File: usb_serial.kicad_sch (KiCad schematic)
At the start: 3 parts, among them U5 CP2104-F03-GM

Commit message: laid out stuff
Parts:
- added C17, C18: 1uF, Capacitor_SMD:C_0805_2012Metric_Pad1.18x1.45mm_HandSolder, symbol Device:C
- U5: Availability In Stock -> (none); Check_prices https://www.snapeda.com/parts/CP2104-F03-GM/Silicon+Labs/vi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 -> (none); MANUFACTURER Silicon Labs -> (none); MF Silicon Labs -> (none); MP CP2104-F03-GM -> (none); PARTREV 1.2 -> (none); Package QFN-24 Silicon Labs -> (none); Price None -> (none); Purchase-URL https://www.snapeda.com/api/url_track_click_mouser/?unipart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 -> (none); STANDARD IPC7351B -> (none); SnapEDA_Link https://www.snapeda.com/parts/CP2104-F03-GM/Silicon+Labs/vi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 -> (none)
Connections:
- net +5V: now also U5.7 (REGIN), C18.1
- net GND: now also C17.2, C18.2
- net at U5.16 (VPP): now also C17.1
- net +3.3V renamed +3V3
- net +3V3: no longer U5.7 (REGIN)
- no-connect marks 12 -> 11
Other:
- note added: "Note: +3V3 is for the CP2104 ONLY, +3.3V is for the ESP32 ONLY"
- moved on the sheet: C10, C9

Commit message: neat-ified schematics
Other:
- company: (none) -> The Art and Science of PCB Design
- title: (none) -> RGB LED Driver Demo Board
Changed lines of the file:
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@@
   (paper "USLetter")
   (title_block
+    (title "RGB LED Driver Demo Board")
     (date "2024-01-01")
     (rev "A01")
+    (company "The Art and Science of PCB Design")
   )
   (junction (at 113.665 71.12) (diameter 0) (color 0 0 0 0)

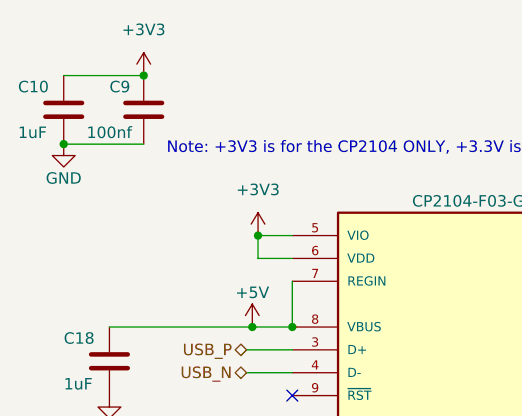
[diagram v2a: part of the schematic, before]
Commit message: Added annotations, BOM count reduction
LED indicator resistors edited to save on BOM count

schematics made more neat, added some labels
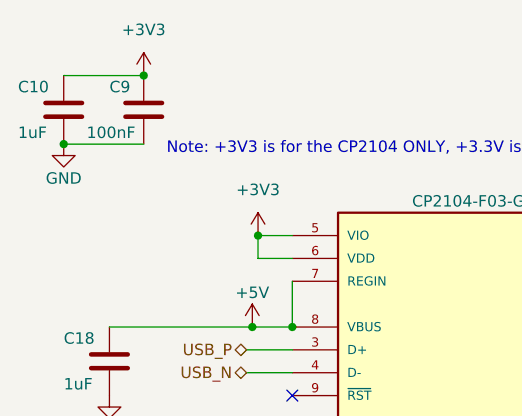
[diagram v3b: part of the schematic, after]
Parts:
- C9: value 100nf -> 100nF
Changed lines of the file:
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@@
       (effects (font (size 1.27 1.27)) (justify left))
     )
-    (property "Value" "100nf" (at 95.25 49.53 0)
+    (property "Value" "100nF" (at 95.25 49.53 0)
       (effects (font (size 1.27 1.27)) (justify left))
     )

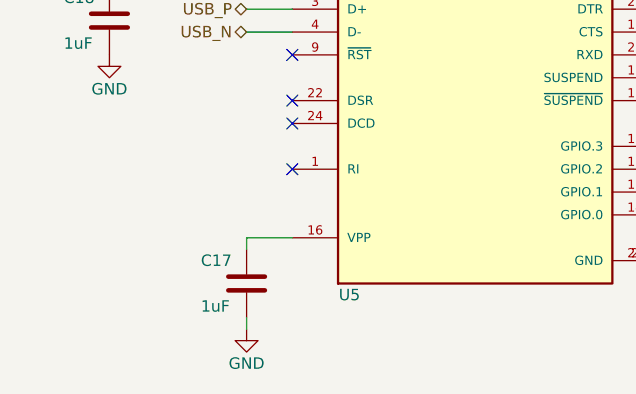
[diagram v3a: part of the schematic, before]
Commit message: added digikey PNs
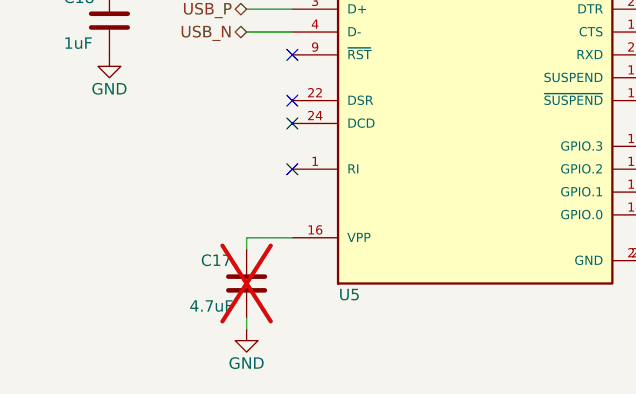
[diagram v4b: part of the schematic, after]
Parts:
- C10, C18, C9: Digikey PN (none) -> 1276-1003-1-ND; MPN (none) -> CL21B104KBCNNNC
- C17: value 1uF -> 4.7uF; Digikey PN (none) -> 445-5980-1-ND; MPN (none) -> C2012X5R1H475K125AB; now not fitted
- U5: Digikey PN (none) -> 336-4146-1-ND; MPN (none) -> CP2104-F03-GM
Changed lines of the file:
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@@
       (effects (font (size 1.27 1.27)) hide)
     )
-    (property "Digikey PN" "" (at 101.6 46.99 0)
+    (property "Digikey PN" "1276-1003-1-ND" (at 101.6 46.99 0)
+      (effects (font (size 1.27 1.27)) hide)
+    )
+    (property "MPN" "CL21B104KBCNNNC" (at 101.6 46.99 0)
       (effects (font (size 1.27 1.27)) hide)
     )
@@
       (effects (font (size 1.27 1.27)) hide)
     )
-    (property "Digikey PN" "" (at 138.43 81.28 0)
+    (property "Digikey PN" "336-4146-1-ND" (at 138.43 81.28 0)
+      (effects (font (size 1.27 1.27)) hide)
+    )
+    (property "MPN" "CP2104-F03-GM" (at 138.43 81.28 0)
       (effects (font (size 1.27 1.27)) hide)
     )
@@
       (effects (font (size 1.27 1.27)) hide)
     )
-    (property "Digikey PN" "" (at 92.71 46.99 0)
+    (property "Digikey PN" "1276-1003-1-ND" (at 92.71 46.99 0)
+      (effects (font (size 1.27 1.27)) hide)
+    )
+    (property "MPN" "CL21B104KBCNNNC" (at 92.71 46.99 0)
       (effects (font (size 1.27 1.27)) hide)
     )
@@
       (effects (font (size 1.27 1.27)) hide)
     )
-    (property "Digikey PN" "" (at 97.79 74.93 0)
+    (property "Digikey PN" "1276-1003-1-ND" (at 97.79 74.93 0)
+      (effects (font (size 1.27 1.27)) hide)
+    )
+    (property "MPN" "CL21B104KBCNNNC" (at 97.79 74.93 0)
       (effects (font (size 1.27 1.27)) hide)
     )
@@
   )
   (symbol (lib_id "Device:C") (at 113.03 104.14 0) (unit 1)
-    (in_bom yes) (on_board yes) (dnp no)
+    (in_bom yes) (on_board yes) (dnp yes)
     (property "Reference" "C17" (at 107.95 101.6 0)
       (effects (font (size 1.27 1.27)) (justify left))
     )
-    (property "Value" "1uF" (at 107.95 106.68 0)
+    (property "Value" "4.7uF" (at 106.68 106.68 0)
       (effects (font (size 1.27 1.27)) (justify left))
     )
@@
       (effects (font (size 1.27 1.27)) hide)
     )
-    (property "Digikey PN" "" (at 113.03 104.14 0)
-      (effects (font (size 1.27 1.27)) hide)
-    )
+    (property "Digikey PN" "445-5980-1-ND" (at 113.03 104.14 0)
+      (effects (font (size 1.27 1.27)) hide)
+    )
+    (property "MPN" "C2012X5R1H475K125AB" (at 113.03 104.14 0)
+      (effects (font (size 1.27 1.27)) hide)
+    )

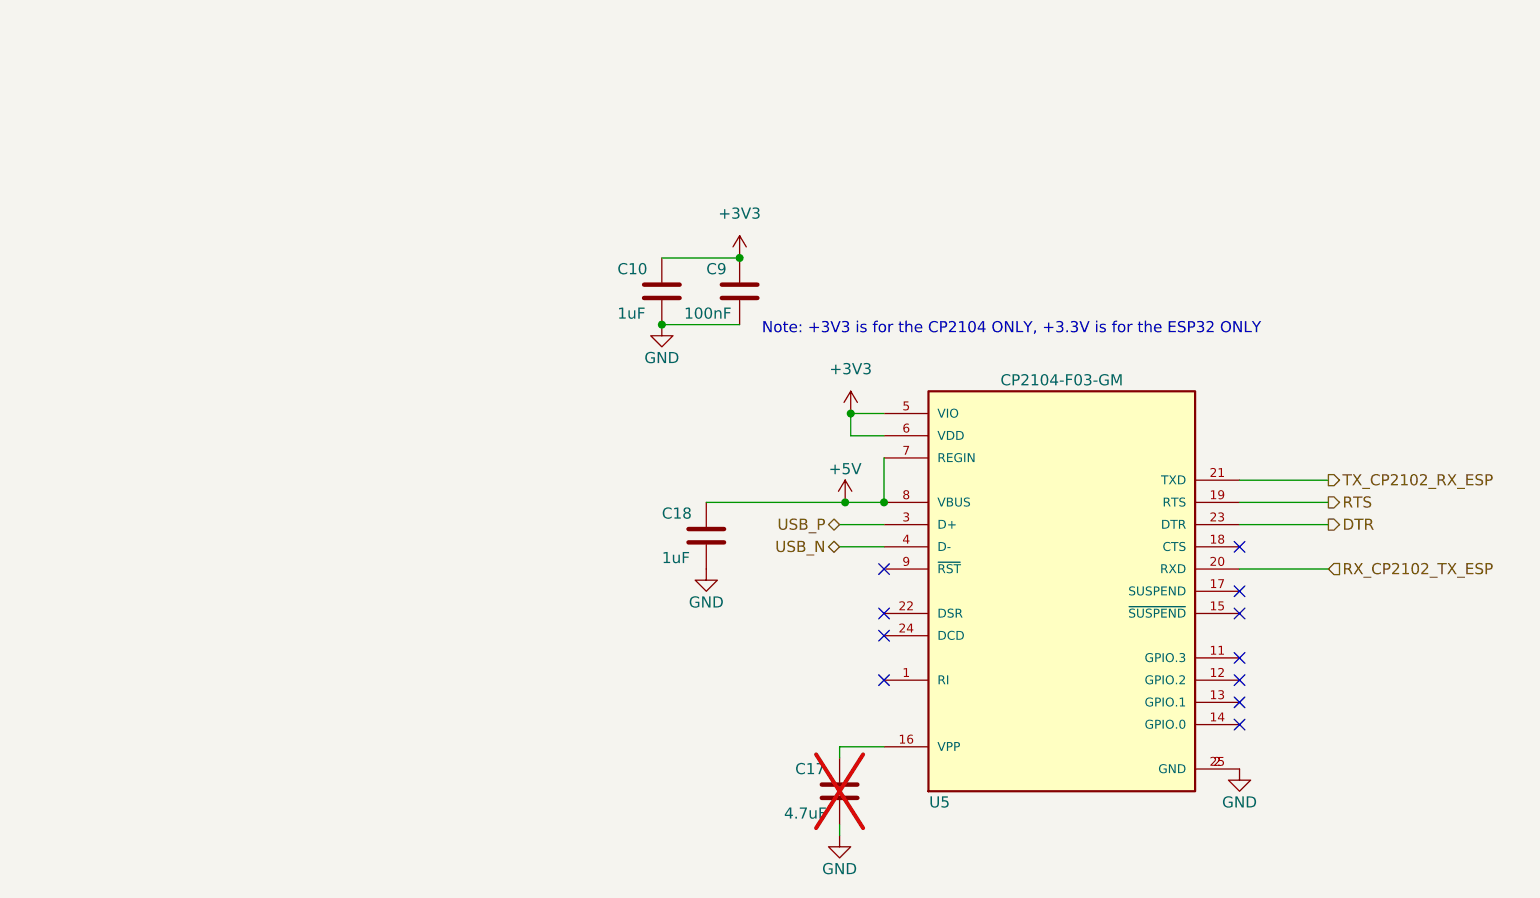
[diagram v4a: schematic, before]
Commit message: [A02] Initial release
CP2014 -> CP2012N (BOM cost reduction)
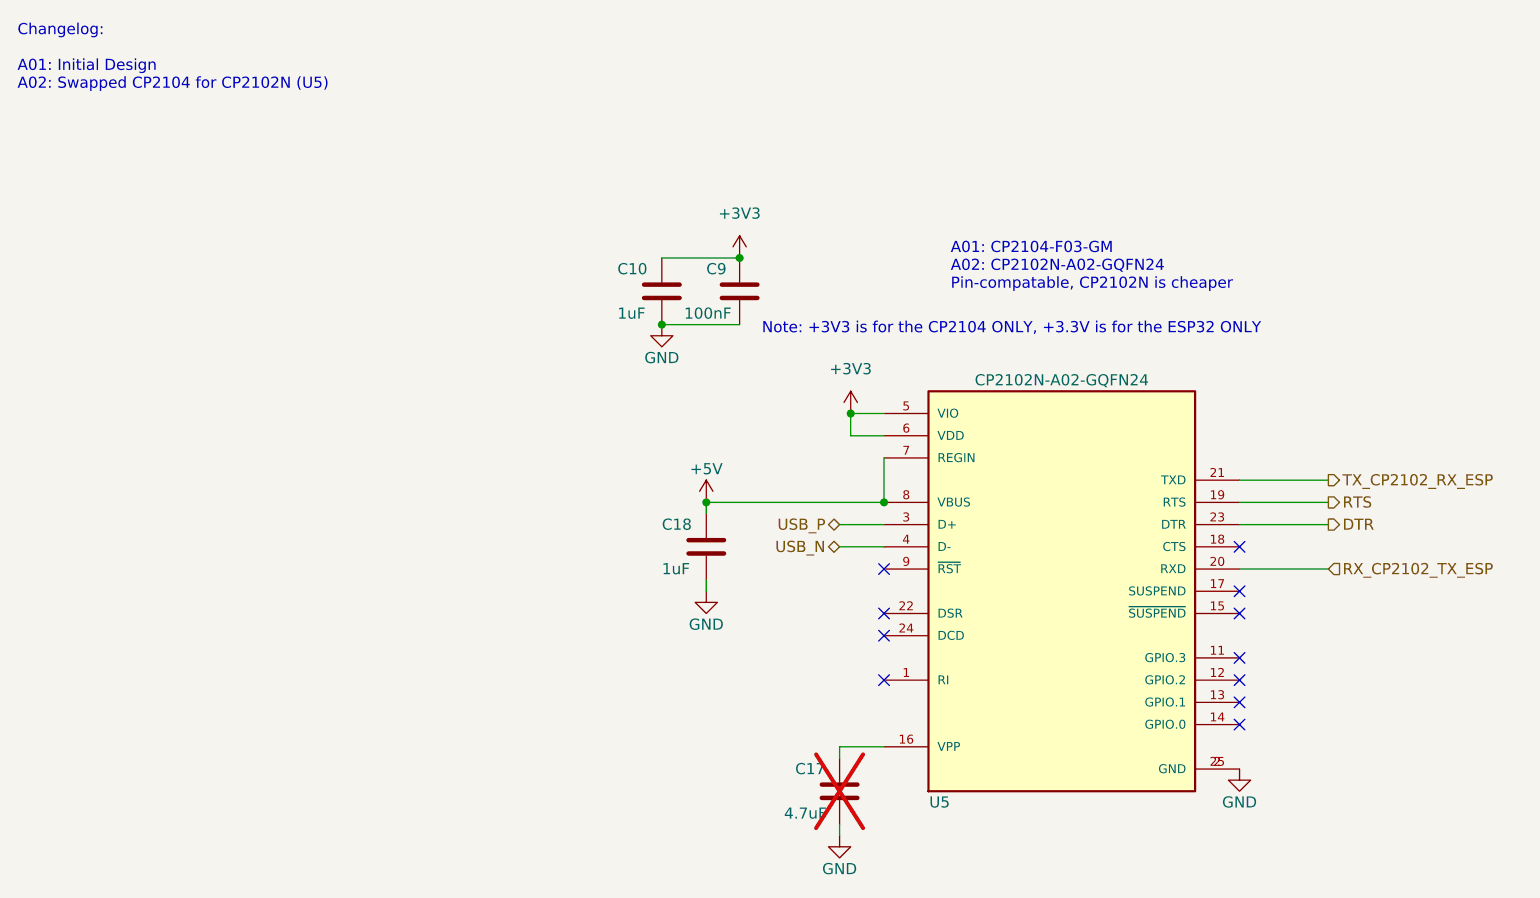
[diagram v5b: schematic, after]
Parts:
- U5: value CP2104-F03-GM -> CP2102N-A02-GQFN24; MPN CP2104-F03-GM -> CP2102N-A02-GQFN24
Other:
- note added: "A01: CP2104-F03-GM A02: CP2102N-A02-GQFN24 Pin-compatable, CP2102N is cheaper"
- note added: "Changelog: A01: Initial Design A02: Swapped CP2104 for CP2102N (U5)"
- moved on the sheet: C18
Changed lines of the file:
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@@
   (title_block
     (title "RGB LED Driver Demo Board")
-    (date "2024-01-01")
-    (rev "A01")
+    (date "2024-01-02")
+    (rev "A02")
     (company "The Art and Science of PCB Design")
   )
-  (junction (at 113.665 71.12) (diameter 0) (color 0 0 0 0)
-  )
   (junction (at 92.71 50.8) (diameter 0) (color 0 0 0 0)
   )
@@
   )
   (junction (at 118.11 71.12) (diameter 0) (color 0 0 0 0)
+  )
+  (junction (at 97.79 71.12) (diameter 0) (color 0 0 0 0)
   )
   (no_connect (at 158.75 76.2))
@@
     (stroke (width 0) (type default))
   )
-  (wire (pts (xy 113.665 71.12) (xy 118.11 71.12))
+  (wire (pts (xy 97.79 71.12) (xy 118.11 71.12))
     (stroke (width 0) (type default))
   )
@@
     (stroke (width 0) (type default))
   )
-  (wire (pts (xy 97.79 71.12) (xy 113.665 71.12))
+  (wire (pts (xy 97.79 72.39) (xy 97.79 71.12))
     (stroke (width 0) (type default))
   )
   (wire (pts (xy 158.75 78.74) (xy 168.91 78.74))
+    (stroke (width 0) (type default))
+  )
+  (wire (pts (xy 97.79 81.28) (xy 97.79 80.01))
     (stroke (width 0) (type default))
   )
@@
     (effects (font (size 1.27 1.27)) (justify left bottom))
   )
+  (text "A01: CP2104-F03-GM\nA02: CP2102N-A02-GQFN24\nPin-compatable, CP2102N is cheaper"
+    (at 125.73 46.99 0)
+    (effects (font (size 1.27 1.27)) (justify left bottom))
+  )
+  (text "Changelog:\n\nA01: Initial Design\nA02: Swapped CP2104 for CP2102N (U5)"
+    (at 19.05 24.13 0)
+    (effects (font (size 1.27 1.27)) (justify left bottom))
+  )
   (hierarchical_label "DTR" (shape output) (at 168.91 73.66 0) (fields_autoplaced)
     (effects (font (size 1.27 1.27)) (justify left))
@@
     )
   )
-  (symbol (lib_id "power:GND") (at 97.79 78.74 0) (unit 1)
-    (in_bom yes) (on_board yes) (dnp no)
-    (property "Reference" "#PWR061" (at 97.79 85.09 0)
-      (effects (font (size 1.27 1.27)) hide)
-    )
-    (property "Value" "GND" (at 97.79 82.55 0)
-      (effects (font (size 1.27 1.27)))
-    )
-    (property "Footprint" "" (at 97.79 78.74 0)
-      (effects (font (size 1.27 1.27)) hide)
-    )
-    (property "Datasheet" "" (at 97.79 78.74 0)
+  (symbol (lib_id "power:GND") (at 97.79 81.28 0) (unit 1)
+    (in_bom yes) (on_board yes) (dnp no)
+    (property "Reference" "#PWR061" (at 97.79 87.63 0)
+      (effects (font (size 1.27 1.27)) hide)
+    )
+    (property "Value" "GND" (at 97.79 85.09 0)
+      (effects (font (size 1.27 1.27)))
+    )
+    (property "Footprint" "" (at 97.79 81.28 0)
+      (effects (font (size 1.27 1.27)) hide)
+    )
+    (property "Datasheet" "" (at 97.79 81.28 0)
       (effects (font (size 1.27 1.27)) hide)
     )
@@
     )
   )
-  (symbol (lib_id "power:+5V") (at 113.665 71.12 0) (unit 1)
-    (in_bom yes) (on_board yes) (dnp no)
-    (property "Reference" "#PWR046" (at 113.665 74.93 0)
-      (effects (font (size 1.27 1.27)) hide)
-    )
-    (property "Value" "+5V" (at 113.665 67.31 0)
-      (effects (font (size 1.27 1.27)))
-    )
-    (property "Footprint" "" (at 113.665 71.12 0)
-      (effects (font (size 1.27 1.27)) hide)
-    )
-    (property "Datasheet" "" (at 113.665 71.12 0)
+  (symbol (lib_id "power:+5V") (at 97.79 71.12 0) (unit 1)
+    (in_bom yes) (on_board yes) (dnp no)
+    (property "Reference" "#PWR046" (at 97.79 74.93 0)
+      (effects (font (size 1.27 1.27)) hide)
+    )
+    (property "Value" "+5V" (at 97.79 67.31 0)
+      (effects (font (size 1.27 1.27)))
+    )
+    (property "Footprint" "" (at 97.79 71.12 0)
+      (effects (font (size 1.27 1.27)) hide)
+    )
+    (property "Datasheet" "" (at 97.79 71.12 0)
       (effects (font (size 1.27 1.27)) hide)
     )
@@
       (effects (font (size 1.27 1.27)))
     )
-    (property "Value" "CP2104-F03-GM" (at 138.43 57.15 0)
+    (property "Value" "CP2102N-A02-GQFN24" (at 138.43 57.15 0)
       (effects (font (size 1.27 1.27)))
     )
@@
       (effects (font (size 1.27 1.27)) (justify bottom) hide)
     )
-    (property "Datasheet" "" (at 138.43 81.28 0)
+    (property "Datasheet" "https://www.silabs.com/documents/public/data-sheets/cp2102n-datasheet.pdf" (at 138.43 81.28 0)
       (effects (font (size 1.27 1.27)) hide)
     )
@@
       (effects (font (size 1.27 1.27)) hide)
     )
-    (property "MPN" "CP2104-F03-GM" (at 138.43 81.28 0)
+    (property "MPN" "CP2102N-A02-GQFN24" (at 138.43 81.28 0)
       (effects (font (size 1.27 1.27)) hide)
     )
@@
     )
   )
-  (symbol (lib_id "Device:C") (at 97.79 74.93 0) (unit 1)
-    (in_bom yes) (on_board yes) (dnp no)
-    (property "Reference" "C18" (at 92.71 72.39 0)
-      (effects (font (size 1.27 1.27)) (justify left))
-    )
-    (property "Value" "1uF" (at 92.71 77.47 0)
-      (effects (font (size 1.27 1.27)) (justify left))
-    )
-    (property "Footprint" "Capacitor_SMD:C_0805_2012Metric_Pad1.18x1.45mm_HandSolder" (at 98.7552 78.74 0)
-      (effects (font (size 1.27 1.27)) hide)
-    )
-    (property "Datasheet" "~" (at 97.79 74.93 0)
-      (effects (font (size 1.27 1.27)) hide)
-    )
-    (property "Digikey PN" "1276-1003-1-ND" (at 97.79 74.93 0)
-      (effects (font (size 1.27 1.27)) hide)
-    )
-    (property "MPN" "CL21B104KBCNNNC" (at 97.79 74.93 0)
-      (effects (font (size 1.27 1.27)) hide)
-    )
+  (symbol (lib_id "Device:C") (at 97.79 76.2 0) (unit 1)
+    (in_bom yes) (on_board yes) (dnp no)
+    (property "Reference" "C18" (at 92.71 73.66 0)
+      (effects (font (size 1.27 1.27)) (justify left))
+    )
+    (property "Value" "1uF" (at 92.71 78.74 0)
+      (effects (font (size 1.27 1.27)) (justify left))
+    )
+    (property "Footprint" "Capacitor_SMD:C_0805_2012Metric_Pad1.18x1.45mm_HandSolder" (at 98.7552 80.01 0)
+      (effects (font (size 1.27 1.27)) hide)
+    )
+    (property "Datasheet" "~" (at 97.79 76.2 0)
+      (effects (font (size 1.27 1.27)) hide)
+    )
+    (property "Digikey PN" "1276-1003-1-ND" (at 97.79 76.2 0)
+      (effects (font (size 1.27 1.27)) hide)
+    )
+    (property "MPN" "CL21B104KBCNNNC" (at 97.79 76.2 0)
+      (effects (font (size 1.27 1.27)) hide)
+    )

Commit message: cost reduction in BOM
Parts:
- C10, C18: Digikey PN 1276-1003-1-ND -> 1276-1029-1-ND; MPN CL21B104KBCNNNC -> CL21B105KBFNNNE
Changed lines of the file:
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@@
       (effects (font (size 1.27 1.27)) hide)
     )
-    (property "Digikey PN" "1276-1003-1-ND" (at 92.71 46.99 0)
+    (property "Digikey PN" "1276-1029-1-ND" (at 92.71 46.99 0)
       (effects (font (size 1.27 1.27)) hide)
     )
-    (property "MPN" "CL21B104KBCNNNC" (at 92.71 46.99 0)
+    (property "MPN" "CL21B105KBFNNNE" (at 92.71 46.99 0)
       (effects (font (size 1.27 1.27)) hide)
     )
@@
       (effects (font (size 1.27 1.27)) hide)
     )
-    (property "Digikey PN" "1276-1003-1-ND" (at 97.79 76.2 0)
+    (property "Digikey PN" "1276-1029-1-ND" (at 97.79 76.2 0)
       (effects (font (size 1.27 1.27)) hide)
     )
-    (property "MPN" "CL21B104KBCNNNC" (at 97.79 76.2 0)
+    (property "MPN" "CL21B105KBFNNNE" (at 97.79 76.2 0)
       (effects (font (size 1.27 1.27)) hide)
     )
